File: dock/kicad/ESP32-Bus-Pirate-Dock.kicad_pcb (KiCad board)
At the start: 4 copper layers, 80 x 73.8 mm, 40 parts, among them CN1 HX25418-10WA, J1 Conn_01x22, J2 Conn_01x22, J3 Conn_01x10V, J4 Conn_01x22, J5 Conn_01x22, J6 Conn_01x22, J7 Conn_02x03, Q1 2N7002, SW1 TA-3532S-A2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

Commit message: Added LCSC Parts & Board Version to v3
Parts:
- Q1: value 2N7002 -> 2SK2009

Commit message: Added testpoints, J3 mirrored
- J3 mirrored in order to share the same pin numbers with CN1. It just makes it less confusing.

- Added test points on power supplies, and SEL signals just to help test the board.
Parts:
- added TP1: +3.3V, TestPoint:TestPoint_Pad_D1.0mm, F.Cu at (154.4, 119.1)
- added TP2: +1.8V, TestPoint:TestPoint_Pad_D1.0mm, F.Cu at (148.8, 119.1)
- added TP3: +5V, TestPoint:TestPoint_Pad_D1.0mm, F.Cu at (160.0, 119.1)
- added TP4: GND, TestPoint:TestPoint_Pad_D1.0mm, F.Cu at (143.8, 116.1)
- added TP5: VTARGET, TestPoint:TestPoint_Pad_D1.0mm, F.Cu at (139.0, 119.1)
- added TP6: SEL, TestPoint:TestPoint_Pad_D1.0mm, F.Cu at (140.7, 77.7)
- added TP7: ~{SEL}, TestPoint:TestPoint_Pad_D1.0mm, F.Cu at (160.0, 77.0)
- moved J3 22.9 mm to (138.9, 109.2), turned to 180 degrees
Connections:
- J3 pad 1: GND -> VTARGET
- J3 pad 10: VTARGET -> GND
- J3 pad 2: IO15 -> IO13
- J3 pad 3: IO16 -> IO12
- J3 pad 4: IO17 -> IO11
- J3 pad 5: IO18 -> IO10
- J3 pad 6: IO10 -> IO18
- J3 pad 7: IO11 -> IO17
- J3 pad 8: IO12 -> IO16
- J3 pad 9: IO13 -> IO15
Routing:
- net VTARGET: track 79.5 -> 89.4 mm
- net /Voltage Level Translator/~{SEL}: track 60.1 -> 65.6 mm
- net +5V: track 107.1 -> 111.0 mm, vias 3 -> 4
- net +3.3V: track 159.4 -> 163.2 mm, vias 10 -> 11
- net /Voltage Level Translator/SEL: track 85.3 -> 87.9 mm
- net +1V8: track 166.4 -> 168.7 mm, vias 6 -> 7
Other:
- board text added: "GND IO15 IO16 IO17 IO18 IO10 IO11 IO12 IO13 VTarget"
- board text removed: "GND IO15 IO16 IO17 IO18 IO10 IO11 IO12 IO13 VCC"

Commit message: Modified test pads & added TC2050
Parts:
- removed REF**: OSHW-Symbol_6.7x6mm_SilkScreen, Symbol:OSHW-Symbol_6.7x6mm_SilkScreen
- added J8: TC2050, Connector:Tag-Connect_TC2050-IDC-NL_2x05_P1.27mm_Vertical_with_bottom_clip, F.Cu at (140.3, 117.9)
- TP1: value +3.3V -> 3V3
- TP2: value +1.8V -> 1V8
- TP3: value +5V -> 5V
- TP5: value VTARGET -> V_{TARGET}
- moved TP5 49.6 mm to (161.5, 74.9)
- moved TP6 20.4 mm to (160.7, 81.8)
- moved TP2 6.21 mm to (153.2, 114.7)
- moved TP4 5.36 mm to (148.8, 117.9)
- moved TP3 4.65 mm to (160.5, 114.5)
- moved TP7 3.93 mm to (156.6, 78.9)
- moved TP1 2.76 mm to (156.9, 117.9)
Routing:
- net /Voltage Level Translator/SEL: track 87.9 -> 139.8 mm, vias 4 -> 6
- net +5V: track 111.0 -> 137.9 mm, vias 4 -> 5
- net /Voltage Level Translator/~{SEL}: track 65.6 -> 84.3 mm, vias 2 -> 3
- net +3.3V: track 163.2 -> 179.7 mm, vias 11 -> 12
- net +1V8: track 168.7 -> 181.3 mm, vias 7 -> 8
- net VTARGET: track 89.4 -> 98.1 mm, vias 2 -> 4
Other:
- board text added: "DEBUG"

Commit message: Changed VTarget to Vio
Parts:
- TP1: value 3V3 -> +3.3V
- TP2: value 1V8 -> +1.8V
- TP3: value 5V -> +5V
- TP5: value V_{TARGET} -> VIO
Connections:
- net VTARGET renamed VIO
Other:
- board text added: "GND IO15 IO16 IO17 IO18 IO10 IO11 IO12 IO13 VIO"
- board text removed: "GND IO15 IO16 IO17 IO18 IO10 IO11 IO12 IO13 VTarget"
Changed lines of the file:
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@@
 	(net 41 "+1V8")
 	(net 42 "IO15")
-	(net 43 "VTARGET")
+	(net 43 "VIO")
 	(net 44 "IO12")
 	(net 45 "IO17")
@@
 			)
 		)
-		(property "Value" "1V8"
+		(property "Value" "+1.8V"
 			(at 0 1.6 180)
 			(layer "F.SilkS")
@@
 			)
 		)
-		(property "Value" "3V3"
+		(property "Value" "+3.3V"
 			(at 0 1.6 0)
 			(layer "F.SilkS")
@@
 			)
 		)
-		(property "Value" "5V"
+		(property "Value" "+5V"
 			(at 0 1.6 0)
 			(layer "F.SilkS")
@@
 			(size 0.7874 0.7874)
 			(layers "F.Cu" "F.Mask")
-			(net 43 "VTARGET")
+			(net 43 "VIO")
 			(pintype "passive")
 		)
@@
 			(layers "*.Cu" "*.Mask")
 			(remove_unused_layers no)
-			(net 43 "VTARGET")
+			(net 43 "VIO")
 			(pinfunction "1")
 			(pintype "unspecified")
@@
 			(layers "*.Cu" "*.Mask")
 			(remove_unused_layers no)
-			(net 43 "VTARGET")
+			(net 43 "VIO")
 			(pinfunction "Pin_1")
 			(pintype "passive")
@@
 			(size 0.6 1.2)
 			(layers "F.Cu" "F.Mask" "F.Paste")
-			(net 43 "VTARGET")
+			(net 43 "VIO")
 			(pinfunction "NC")
 			(pintype "input")
@@
 			(size 1.2 1.75)
 			(layers "F.Cu" "F.Mask" "F.Paste")
-			(net 43 "VTARGET")
+			(net 43 "VIO")
 			(pinfunction "2")
 			(pintype "unspecified")
@@
 			(layers "F.Cu" "F.Mask" "F.Paste")
 			(roundrect_rratio 0.25)
-			(net 43 "VTARGET")
+			(net 43 "VIO")
 			(pintype "passive")
 		)
@@
 			)
 		)
-		(property "Value" "V_{TARGET}"
+		(property "Value" "VIO"
 			(at 0.5 1.7 0)
 			(layer "F.SilkS")
@@
 			(size 1 1)
 			(layers "F.Cu" "F.Mask")
-			(net 43 "VTARGET")
+			(net 43 "VIO")
 			(pinfunction "1")
 			(pintype "passive")
@@
 		)
 	)
-	(gr_text "GND\n\nIO15\n\nIO16\n\nIO17\n\nIO18\n\nIO10\n\nIO11\n\nIO12\n\nIO13\n\nVTarget"
+	(gr_text "GND\n\nIO15\n\nIO16\n\nIO17\n\nIO18\n\nIO10\n\nIO11\n\nIO12\n\nIO13\n\nVIO"
 		(at 141.9162 110.0932 0)
 		(layer "F.SilkS" knockout)
@@
 		(drill 0.2)
 		(layers "F.Cu" "B.Cu")
+		(free yes)
 		(net 43)
 	)
@@
 		(drill 0.2)
 		(layers "F.Cu" "B.Cu")
+		(free yes)
 		(net 43)
 	)
@@
 		(drill 0.2)
 		(layers "F.Cu" "B.Cu")
+		(free yes)
 		(net 43)
 	)
@@
 		(drill 0.2)
 		(layers "F.Cu" "B.Cu")
+		(free yes)
 		(net 43)
 	)

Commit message: Re-added "Open Hardware" Logo
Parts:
- added REF**: OSHW-Logo2_9.8x8mm_SilkScreen, Symbol:OSHW-Logo2_9.8x8mm_SilkScreen, F.Cu at (129.6, 73.6)

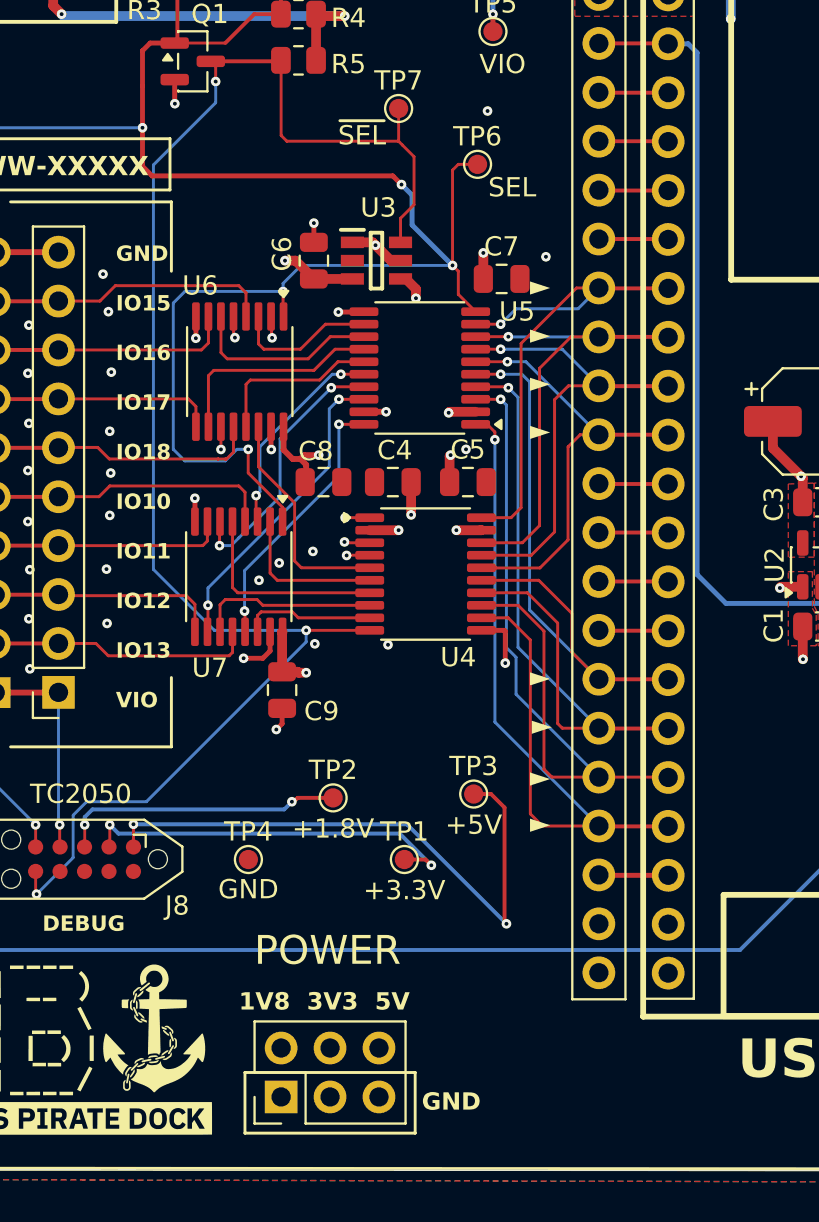
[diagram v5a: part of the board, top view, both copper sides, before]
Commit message: Added OSHW mark
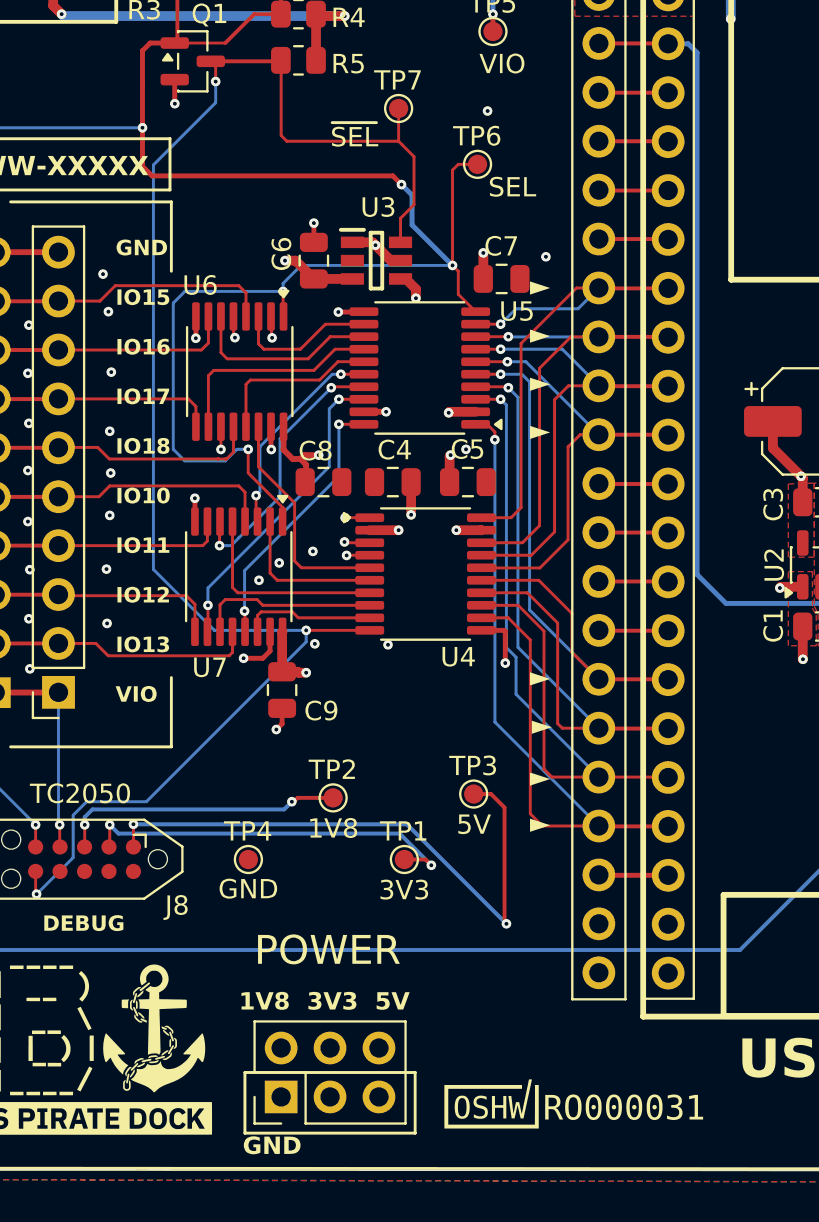
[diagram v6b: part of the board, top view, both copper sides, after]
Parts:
- added G***: LOGO, LOGO, F.Cu at (165.7, 130.6)
- TP1: value +3.3V -> 3V3
- TP2: value +1.8V -> 1V8
- TP3: value +5V -> 5V

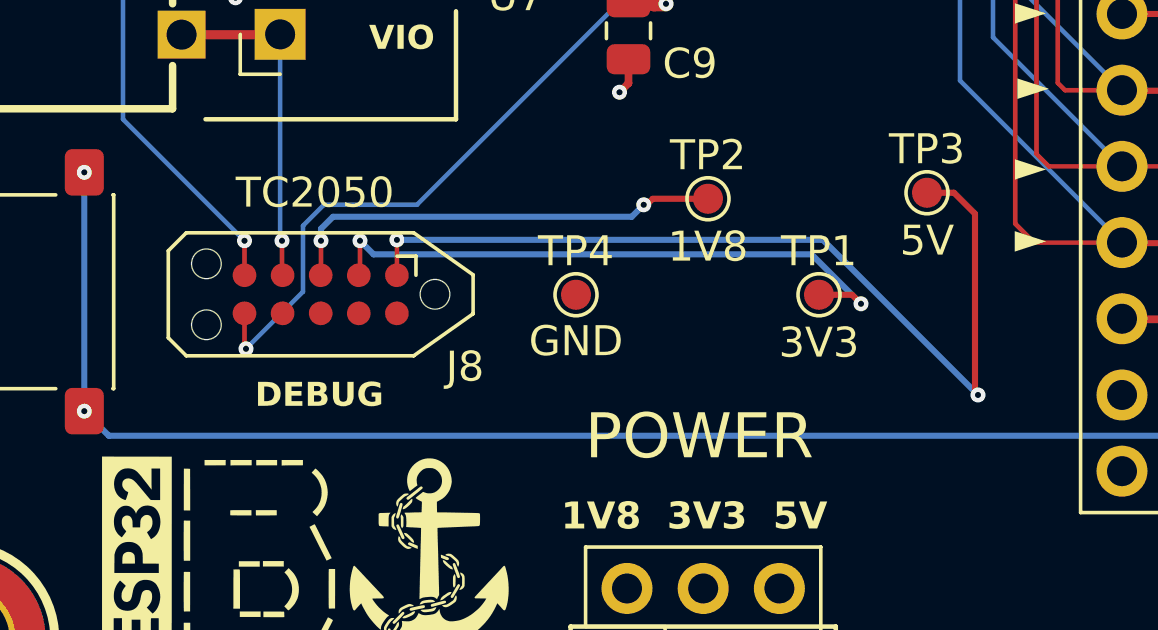
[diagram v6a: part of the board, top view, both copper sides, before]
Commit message: Added PCB dimensions
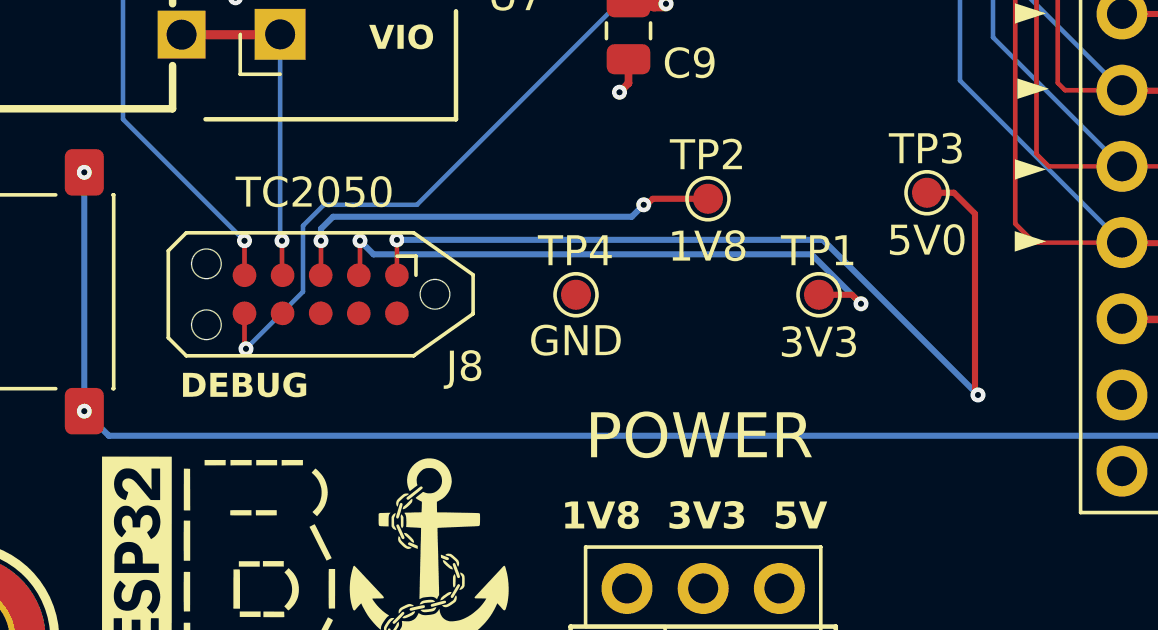
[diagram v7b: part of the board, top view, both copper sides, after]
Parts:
- TP3: value 5V -> 5V0
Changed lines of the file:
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@@
 	(layers
 		(0 "F.Cu" signal)
-		(4 "In1.Cu" signal)
-		(6 "In2.Cu" signal)
+		(4 "In1.Cu" power)
+		(6 "In2.Cu" power)
 		(2 "B.Cu" signal)
 		(13 "F.Paste" user)
@@
 		(1 "F.Mask" user)
 		(3 "B.Mask" user)
+		(19 "Cmts.User" user "User.Comments")
 		(25 "Edge.Cuts" user)
 		(27 "Margin" user)
@@
 			)
 		)
-		(property "Value" "5V"
+		(property "Value" "5V0"
 			(at 0 1.6 0)
 			(layer "F.SilkS")
@@
 	)
 	(gr_text "DEBUG"
-		(at 138.1 121.7 0)
+		(at 135.6 121.4 0)
 		(layer "F.SilkS" knockout)
 		(effects
@@
 			)
 		)
+	)
+	(dimension
+		(type orthogonal)
+		(layer "Cmts.User")
+		(pts
+			(xy 128.3 129.393555) (xy 199.02 129.37)
+		)
+		(height 14.406445)
+		(orientation 0)
+		(format
+			(prefix "")
+			(suffix "")
+			(units 3)
+			(units_format 0)
+			(precision 4)
+			(suppress_zeroes yes)
+		)
+		(style
+			(thickness 0.1)
+			(arrow_length 1.27)
+			(text_position_mode 0)
+			(arrow_direction outward)
+			(extension_height 0.58642)
+			(extension_offset 0.5)
+			(keep_text_aligned yes)
+		)
+		(gr_text "70,72"
+			(at 163.66 142.65 0)
+			(layer "Cmts.User")
+			(effects
+				(font
+					(size 1 1)
+					(thickness 0.15)
+				)
+			)
+		)
+	)
+	(dimension
+		(type orthogonal)
+		(layer "Cmts.User")
+		(pts
+			(xy 123.7 66.8) (xy 203.7 66.8)
+		)
+		(height -13.2)
+		(orientation 0)
+		(format
+			(prefix "")
+			(suffix "")
+			(units 3)
+			(units_format 0)
+			(precision 4)
+			(suppress_zeroes yes)
+		)
+		(style
+			(thickness 0.1)
+			(arrow_length 1.27)
+			(text_position_mode 0)
+			(arrow_direction outward)
+			(extension_height 0.58642)
+			(extension_offset 0.5)
+			(keep_text_aligned yes)
+		)
+		(gr_text "80"
+			(at 163.7 52.45 0)
+			(layer "Cmts.User")
+			(effects
+				(font
+					(size 1 1)
+					(thickness 0.15)
+				)
+			)
+		)
+	)
+	(dimension
+		(type orthogonal)
+		(layer "Cmts.User")
+		(pts
+			(xy 169.33 125.07) (xy 194.78 125.12)
+		)
+		(height 14.03)
+		(orientation 0)
+		(format
+			(prefix "")
+			(suffix "")
+			(units 3)
+			(units_format 0)
+			(precision 4)
+			(suppress_zeroes yes)
+		)
+		(style
+			(thickness 0.1)
+			(arrow_length 1.27)
+			(text_position_mode 0)
+			(arrow_direction outward)
+			(extension_height 0.58642)
+			(extension_offset 0.5)
+			(keep_text_aligned yes)
+		)
+		(gr_text "25,45"
+			(at 182.055 137.95 0)
+			(layer "Cmts.User")
+			(effects
+				(font
+					(size 1 1)
+					(thickness 0.15)
+				)
+			)
+		)
+	)
+	(dimension
+		(type orthogonal)
+		(layer "Cmts.User")
+		(pts
+			(xy 169.3 125.56) (xy 197.38 125.1)
+		)
+		(height 15.94)
+		(orientation 0)
+		(format
+			(prefix "")
+			(suffix "")
+			(units 3)
+			(units_format 0)
+			(precision 4)
+			(suppress_zeroes yes)
+		)
+		(style
+			(thickness 0.1)
+			(arrow_length 1.27)
+			(text_position_mode 0)
+			(arrow_direction outward)
+			(extension_height 0.58642)
+			(extension_offset 0.5)
+			(keep_text_aligned yes)
+		)
+		(gr_text "28,08"
+			(at 183.34 140.35 0)
+			(layer "Cmts.User")
+			(effects
+				(font
+					(size 1 1)
+					(thickness 0.15)
+				)
+			)
+		)
+	)
+	(dimension
+		(type orthogonal)
+		(layer "Cmts.User")
+		(pts
+			(xy 199.2 134.06202) (xy 199.2 60.29)
+		)
+		(height 11.8)
+		(orientation 1)
+		(format
+			(prefix "")
+			(suffix "")
+			(units 3)
+			(units_format 0)
+			(precision 4)
+			(suppress_zeroes yes)
+		)
+		(style
+			(thickness 0.1)
+			(arrow_length 1.27)
+			(text_position_mode 0)
+			(arrow_direction outward)
+			(extension_height 0.58642)
+			(extension_offset 0.5)
+			(keep_text_aligned yes)
+		)
+		(gr_text "73,772"
+			(at 209.85 97.17601 90)
+			(layer "Cmts.User")
+			(effects
+				(font
+					(size 1 1)
+					(thickness 0.15)
+				)
+			)
+		)
+	)
+	(dimension
+		(type orthogonal)
+		(layer "Cmts.User")
+		(pts
+			(xy 199.2 64.8) (xy 199.02 129.37)
+		)
+		(height 8.3)
+		(orientation 1)
+		(format
+			(prefix "")
+			(suffix "")
+			(units 3)
+			(units_format 0)
+			(precision 4)
+			(suppress_zeroes yes)
+		)
+		(style
+			(thickness 0.1)
+			(arrow_length 1.27)
+			(text_position_mode 0)
+			(arrow_direction outward)
+			(extension_height 0.58642)
+			(extension_offset 0.5)
+			(keep_text_aligned yes)
+		)
+		(gr_text "64,57"
+			(at 206.35 97.085 90)
+			(layer "Cmts.User")
+			(effects
+				(font
+					(size 1 1)
+					(thickness 0.15)
+				)
+			)
+		)
